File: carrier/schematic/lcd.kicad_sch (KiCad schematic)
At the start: 19 parts, among them J15001 AFC07-S40FCA-00, U15001 SY7201ABC, U15002 USBLC6-2SC6

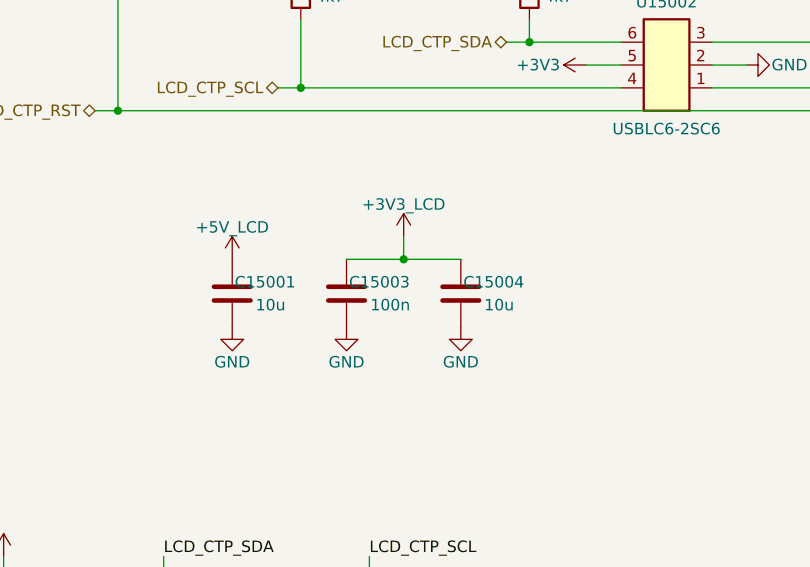
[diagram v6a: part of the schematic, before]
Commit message: fix(audit round-3 / verification pass): regression revert + 6 gaps the re-audit caught
A second independent 65-agent audit of the REMEDIATED board confirmed ZERO
CRITICAL/HIGH (the 3 board-dead fixes held) and surfaced a regression + gaps:

REGRESSION I introduced (caught by re-verify): power_som R18 RT comment said
"~1.5 MHz" — WRONG. RT=22k sets ~600 kHz (SNVSBD5D Eq 2), corroborated by the
folder's own README:43 and the sibling LM61460 cells. I had trusted the FIRST
audit's RT claim; the second audit + the README prove it backwards. Reverted to
600 kHz (resistor value 22k was always correct).

Gaps closed (real):
- lcd: add the dossier-specified 1uF HF bypass (C15849) at the SY7201 boost IN
  (only the 10u bulk was placed). +.cir +test.
- bringup_modules: add a 10k bleed on +3V3_SD (research R5) — SY6280 has no QOD, so
  the SD rail needs a discharge path for power-cycle re-init. +.cir.
- camera: clamp CAM_SCL/CAM_SDA on U2's two SPARE ESD channels (free GND-ref TVS on
  the user-handled FFC I2C lines); CAM_EN/LED stay static-GPIO (documented). +test.
- ratings.py: add the TPD4E1U06 (C124691) TVS row (was UNSPEC fail-soft).
- powertree: remove the dead 'TPS54302' REG_SPECS key (no emitted part uses it,
  BOM-verified) + fix its stale parallel-source comments to LM61460.
- stale docs: bringup_en/.py+README + bringup_en_modules (TPS54302->LM61460 EN),
  rj45 +VLED rationale (the always-on +3V3_SC DOES exist) + README mounting holes,
  som_j2 README (retired FMC_PRSNT_N).

Verified: 148x137, DRC 0, BOARD PASS, POWER TREE PASS (0 findings), golden blessed;
lcd+camera+bringup_modules tests 61/61.

Co-Authored-By: Claude Opus 4.8 <noreply@anthropic.com>
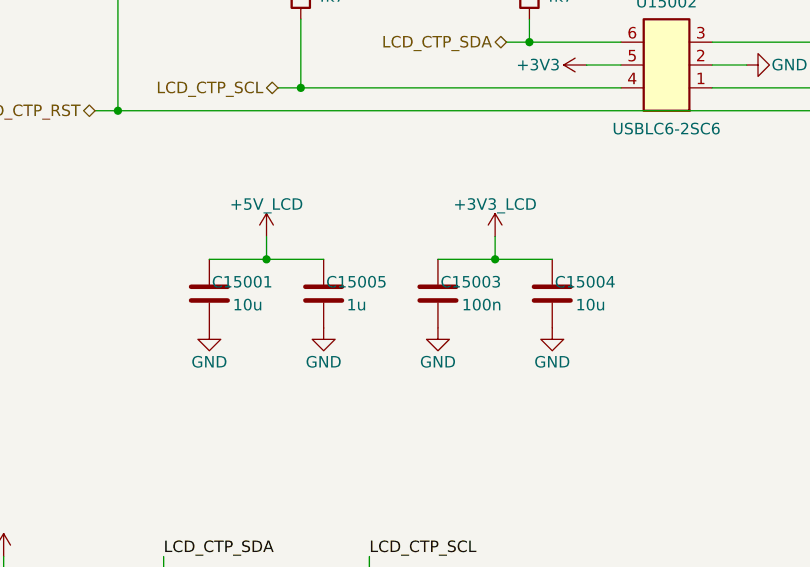
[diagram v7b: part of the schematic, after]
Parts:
- added TP15003: LCD_CTP_SCL, TestPoint:TestPoint_Pad_D1.5mm, symbol Connector:TestPoint
- C15003: renamed from C15004; value 10u -> 100n; footprint Capacitor_SMD:C_0805_2012Metric -> Capacitor_SMD:C_0603_1608Metric; LCSC C15850 -> C14663
- C15004: renamed from TP15001; value +5V_LCD -> 10u; footprint TestPoint:TestPoint_Pad_D1.5mm -> Capacitor_SMD:C_0805_2012Metric; symbol Connector:TestPoint -> Device:C; BOM exclude -> (none); LCSC (none) -> C15850
- C15005: renamed from C15003; value 100n -> 1u; LCSC C14663 -> C15849
- TP15001: renamed from TP15002; value LCD_CTP_SDA -> +5V_LCD
- TP15002: renamed from TP15003; value LCD_CTP_SCL -> LCD_CTP_SDA
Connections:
- net +3V3_LCD: now also C15004.1; no longer C15005.1
- net +5V_LCD: now also C15005.1, TP15001.1; no longer C15004.1
- net GND: now also C15004.2
- net LCD_CTP_SCL: now also TP15003.1; no longer TP15002.1
- net LCD_CTP_SDA: now also TP15002.1; no longer TP15001.1
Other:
- moved on the sheet: C15001, C15003, C15005, TP15001, TP15002
